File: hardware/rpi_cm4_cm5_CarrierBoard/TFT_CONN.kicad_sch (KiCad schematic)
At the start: 36 parts, among them J20 0878325922, J8 62684-402100ALF, J9 5051101092

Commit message: Update watchdog timer circuit to add external watchdog timer IC to be fed by PIC Adjust reset scheme in power supply sheet accordingly Adjust PinMux, regen BOM and PDF schematics (preliminary) Start preliminary component placement in the PCB
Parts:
- removed R132: 0R, footprint:RES_0603, symbol KicadCompDb:Resistors/RES_SMT_00021
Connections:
- net GND: now also J8.11 (GND), J8.31 (GND); no longer J8.10 (GND), J8.30 (GND)
- net LVDS_A.CLK_N: now also D22.1 (I/O1), J8.24 (CLK_N); no longer D22.4 (I/O3), J8.17 (CLK_N)
- net LVDS_A.CLK_P: now also D22.2 (I/O2), J8.23 (CLK_P); no longer D22.5 (I/O4), J8.18 (CLK_P)
- net LVDS_A.D0_N: now also J8.33 (RD0_N); no longer J8.8 (RD0_N)
- net LVDS_A.D0_P: now also J8.32 (RD0_P); no longer J8.9 (RD0_P)
- net LVDS_A.D1_N: now also J8.30 (RD1_N); no longer J8.11 (RD1_N)
- net LVDS_A.D1_P: now also J8.29 (RD1_P); no longer J8.12 (RD1_P)
- net LVDS_A.D2_N: now also J8.27 (RD2_N); no longer J8.14 (RD2_N)
- net LVDS_A.D2_P: now also J8.26 (RD2_P); no longer J8.15 (RD2_P)
- net LVDS_A.D3_N: now also D22.4 (I/O3), J8.21 (RD3_N); no longer D22.1 (I/O1), J8.20 (RD3_N)
- net LVDS_A.D3_P: now also D22.5 (I/O4), J8.20 (RD3_P); no longer D22.2 (I/O2), J8.21 (RD3_P)
- net TFT_AVDD: now also J8.12 (AVDD); no longer J8.29 (AVDD)
- net TFT_LED+: now also J8.1 (LED+), J8.2 (LED+); no longer J8.39 (LED+), J8.40 (LED+)
- net TFT_LED-: now also J8.10 (LED-), J8.9 (LED-); no longer J8.31 (LED-), J8.32 (LED-)
- net TFT_STBYB: now also J8.35 (STBYB); no longer J8.6 (STBYB)
- net TFT_VCOM: now also J8.40 (VCOM); no longer J8.1 (VCOM)
- net TFT_VDD: now also J8.38 (VDD), J8.39 (VDD), J8.8 (L/R); no longer J8.2 (VDD), J8.3 (VDD), J8.33 (L/R)
- net TFT_VGH: now also J8.3 (VGH); no longer J8.38 (VGH)
- net TFT_VGL: now also J8.6 (VGL); no longer J8.35 (VGL)
- net TFT_~{RESET}: now also J8.36 (~{RESET}); no longer J8.5 (~{RESET})
- no-connect marks 4 -> 5
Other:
- note added: "Conn pin 1 = RVT pin 10 Conn pin 10 = RVT pin 1"
- note added: "Conn pin 1 = RVT pin 40 Conn pin 40 = RVT pin 1"
- note added: "Floating hole Close to power-in"

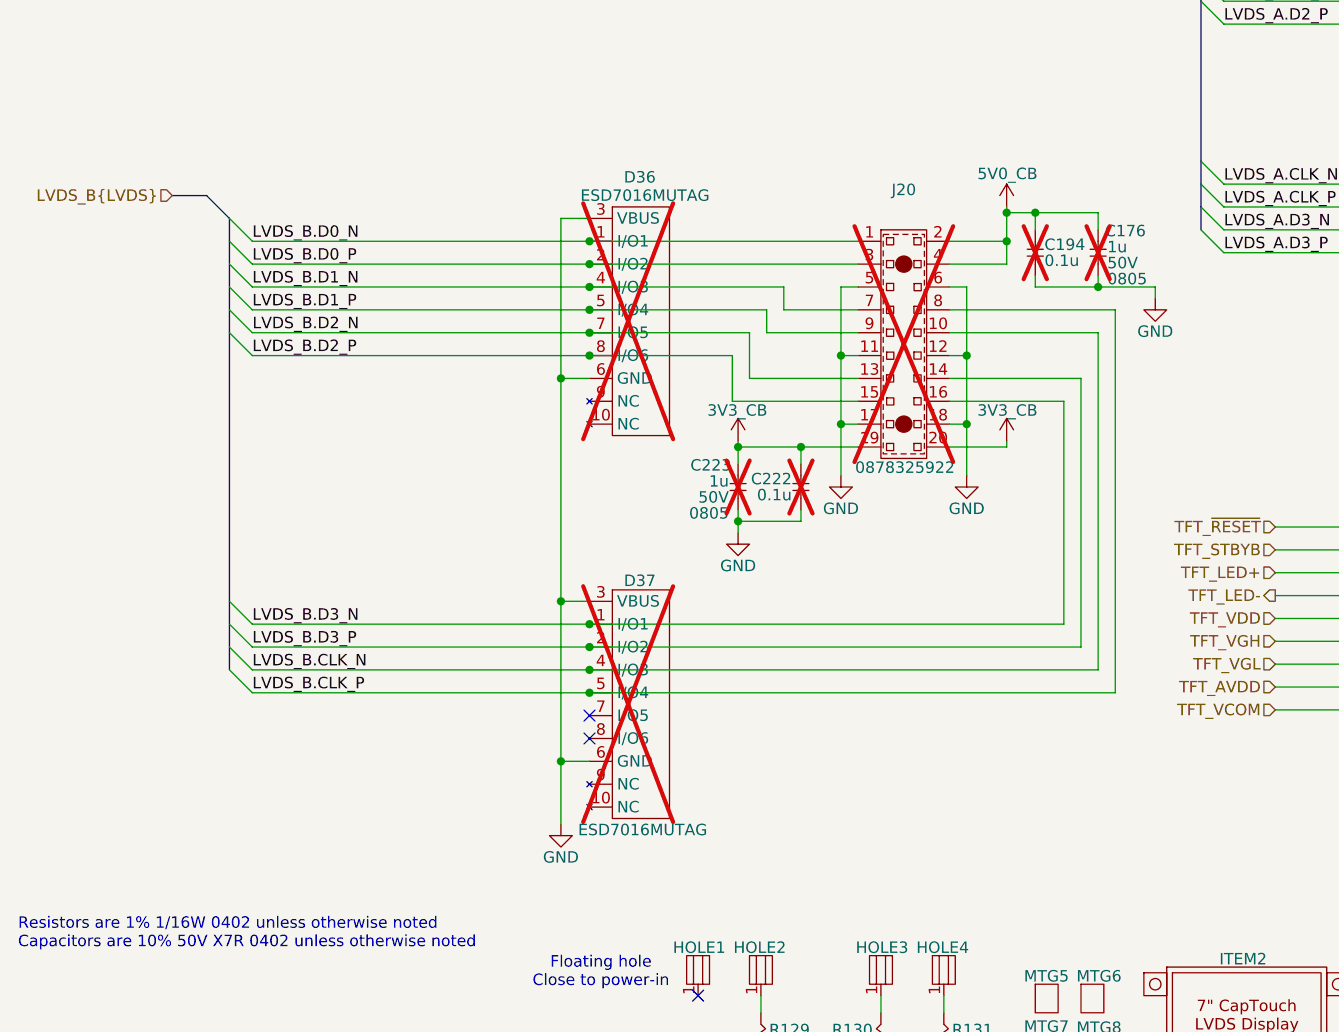
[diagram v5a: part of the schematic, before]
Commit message: Update schematics based on PCB preliminary placement Add preliminary design rules to PCB
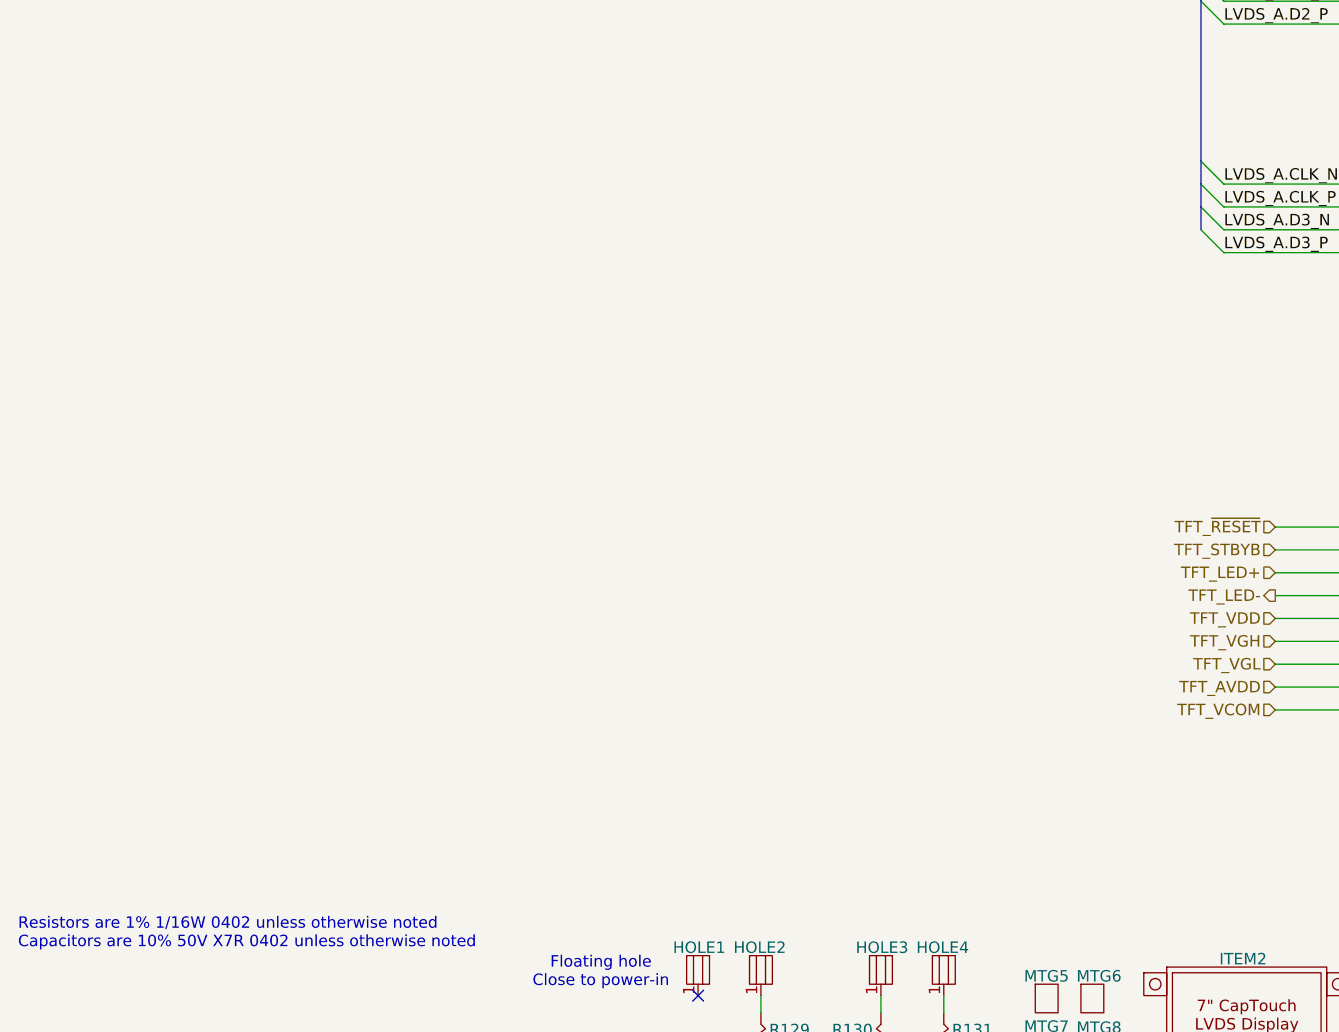
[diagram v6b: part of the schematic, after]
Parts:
- removed C176, C223: 1u, footprint:CAP_NONPOL_0805, symbol KicadCompDb:Capacitors/CAP_CER_SMT_00002
- removed C194, C222: 0.1u, footprint:CAP_NONPOL_0402, symbol KicadCompDb:Capacitors/CAP_CER_SMT_00001
- removed D36, D37: ESD7016MUTAG, footprint:UDFN8, symbol KicadCompDb:ESD Diodes/ESD_DIODE_00001
- removed J20: 0878325922, footprint:0878325922, symbol KicadCompDb:Connector/CONN_00020
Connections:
- no-connect marks 5 -> 3

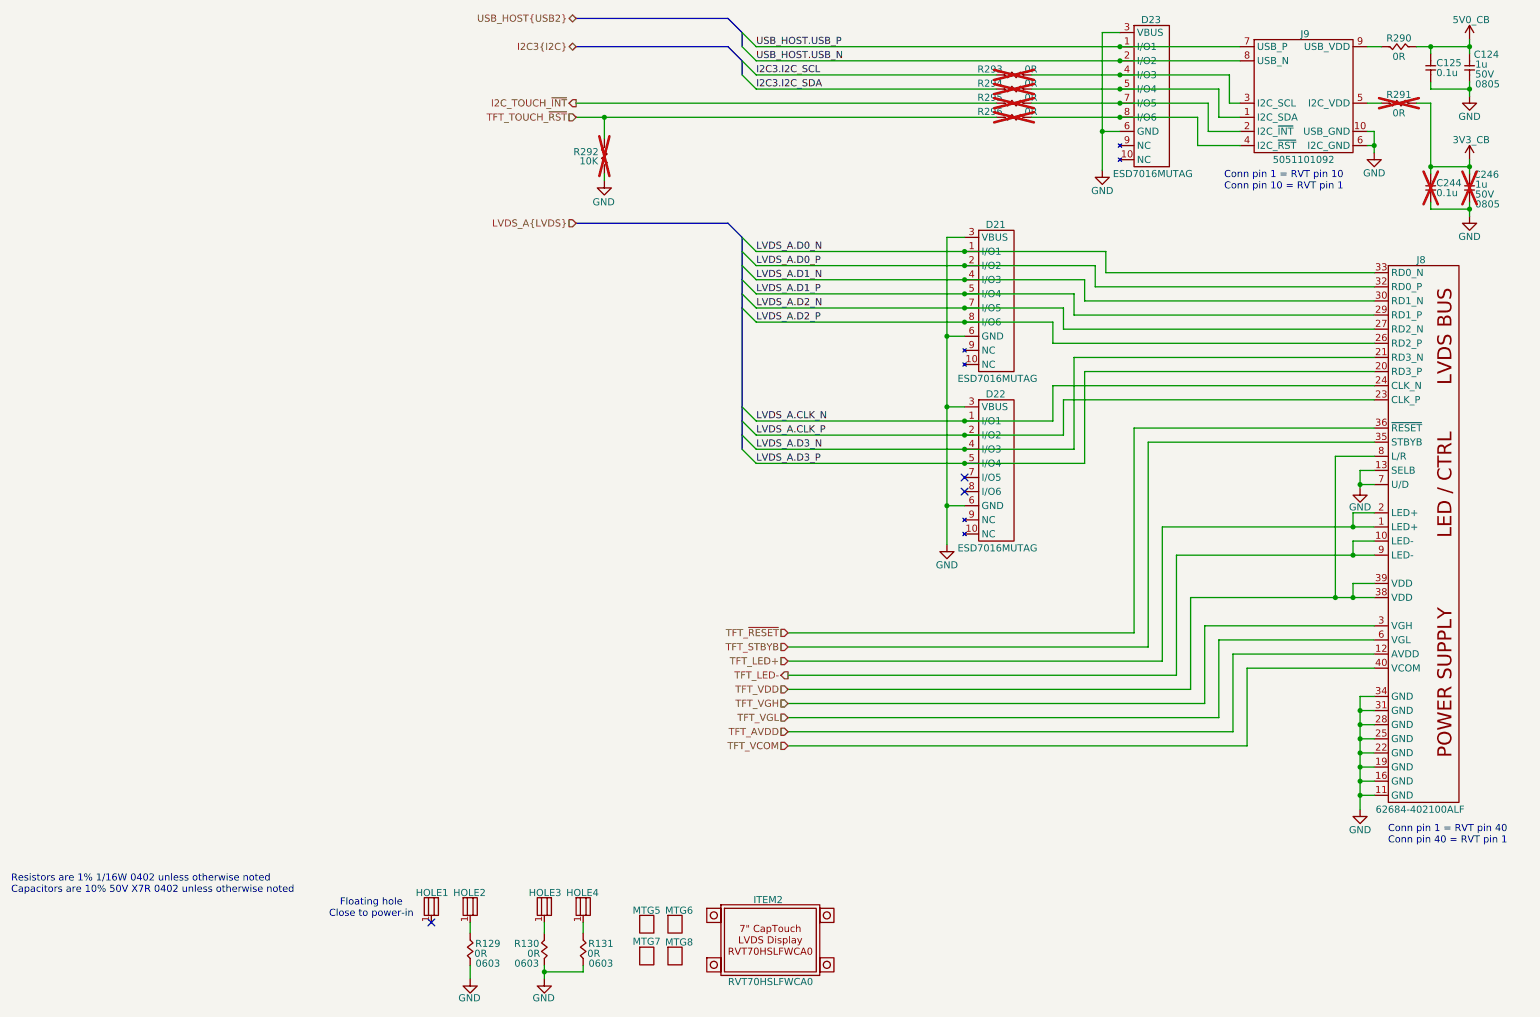
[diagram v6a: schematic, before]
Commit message: Update preliminary placement, update DNP, regen BOM + Preliminary schematics
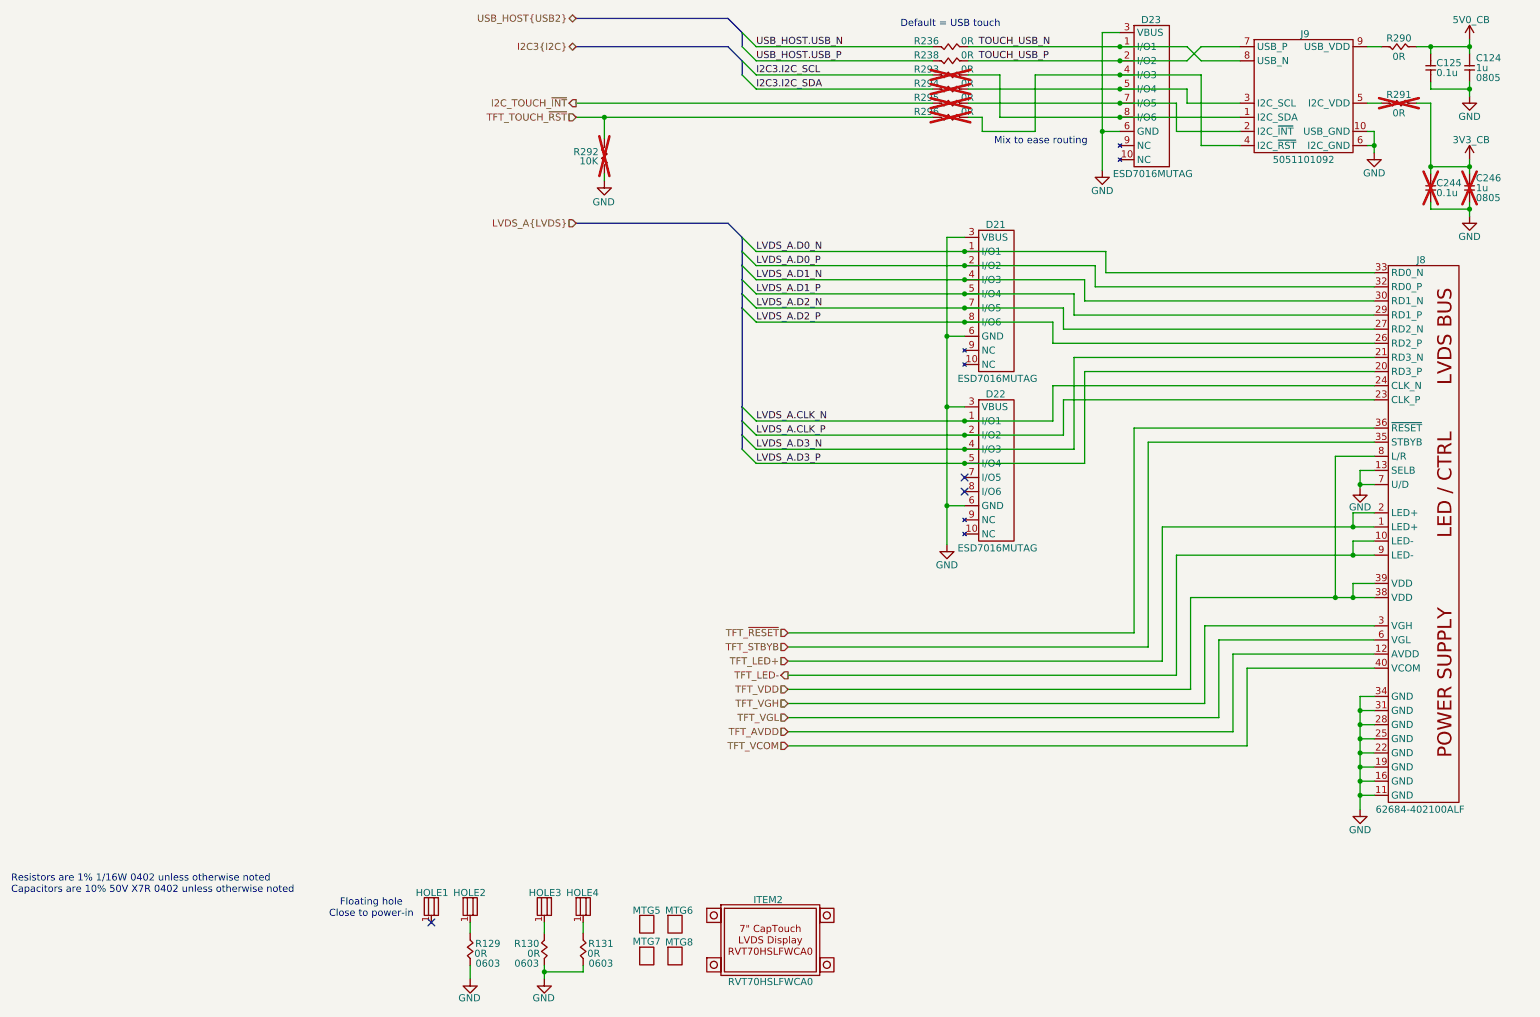
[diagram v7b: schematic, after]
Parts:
- added R236, R238: 0R, footprint:RES_0402, symbol KicadCompDb:Resistors/RES_SMT_00001
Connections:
- net USB_HOST.USB_N: now also R236.2; no longer D23.2 (I/O2), J9.8 (USB_N)
- net USB_HOST.USB_P: now also R238.2; no longer D23.1 (I/O1), J9.7 (USB_P)
- net at J9.4 (I2C_~{RST}), R296.1: now also D23.4 (I/O3); no longer D23.8 (I/O6)
- net at D23.5 (I/O4), R294.1: now also J9.3 (I2C_SCL); no longer J9.1 (I2C_SDA)
- new net: D23.8 (I/O6), J9.1 (I2C_SDA), R293.1
- new net TOUCH_USB_N: D23.1 (I/O1), J9.8 (USB_N), R236.1
- new net TOUCH_USB_P: D23.2 (I/O2), J9.7 (USB_P), R238.1
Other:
- note added: "Default = USB touch"
- note added: "Mix to ease routing"
- note removed: "Conn pin 1 = RVT pin 10 Conn pin 10 = RVT pin 1"
- note removed: "Conn pin 1 = RVT pin 40 Conn pin 40 = RVT pin 1"
- moved on the sheet: R293, R294, R295, R296
